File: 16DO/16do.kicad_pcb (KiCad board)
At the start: 2 copper layers, 170 x 80 mm, 70 parts, among them J1 Conn_02x16_Row_Letter_First, J2 CONN_01X16, J3 CONN_01X16, J4 CONN_01X16, J5 CONN_01X16, P1 CONN_01X08, P2 CONN_01X08, P3 CONN_01X08, P4 CONN_01X08, U1 STM32F030CCTx, U13 74HC595, U14 74HC595, U15 74HC595, U16 74HC595, U2 MC33879A, U3 MC33879A, U4 LD3985G33R_TSOT23, U5 AP1117-33, U6 SP3485, U7 SP3485, U8 SP3485, U9 SP3485, Y1 Crystal_GND3

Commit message: finish leds, route most stuff
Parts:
- added C10: 100n, stmbl:C_0603, F.Cu at (90.8, 33.4)
- added C11: 2.2µ, stmbl:C_0603, F.Cu at (86.9, 38.4)
- added C12: 10µ, stmbl:C_0805, F.Cu at (103.4, 65.4)
- added C13: 10µ, stmbl:C_0805, F.Cu at (91.3, 65.0)
- added C14: 100n, stmbl:C_0603, F.Cu at (126.7, 55.6)
- added C15: 2.2µ, stmbl:C_0603, F.Cu at (109.5, 63.4)
- added C16: 10µ, stmbl:C_0805, F.Cu at (101.1, 65.4)
- added C17: 10µ, stmbl:C_0805, F.Cu at (96.8, 83.0)
- added C18: 100n, stmbl:C_0603, F.Cu at (123.2, 64.8)
- added C19: 100n, stmbl:C_0603, F.Cu at (94.5, 33.4)
- added C20: 100n, stmbl:C_0603, F.Cu at (90.5, 38.0)
- added C21: 100n, stmbl:C_0603, F.Cu at (114.4, 54.0)
- added C22: 100n, stmbl:C_0603, F.Cu at (94.5, 35.6)
- added C7: 100n, stmbl:C_0603, F.Cu at (91.3, 57.4)
- added C8: 2.2µ, stmbl:C_0603, F.Cu at (91.3, 56.1)
- added C9: 100n, stmbl:C_0603, F.Cu at (86.0, 60.2)
- added D24: SS34A, stmbl:SMA_Standard, F.Cu at (88.3, 62.8)
- added L1: 4.7µH 1.5A, stmbl:SMD_INDUCTOR_32x25, F.Cu at (91.3, 61.0)
- added MK11: Mounting_Hole, MountingHole:MountingHole_3.2mm_M3, F.Cu at (80.1, 126.0)
- added MK12: Mounting_Hole, MountingHole:MountingHole_3.2mm_M3, F.Cu at (80.1, 54.0)
- added R10: R, stmbl:R_0603, B.Cu at (178.2, 91.0)
- added R11: R, stmbl:R_0603, B.Cu at (178.8, 93.5)
- added R12: R, stmbl:R_0603, B.Cu at (179.5, 91.0)
- added R13: R, stmbl:R_0603, B.Cu at (180.1, 93.5)
- added R14: R, stmbl:R_0603, B.Cu at (180.8, 91.0)
- added R15: R, stmbl:R_0603, B.Cu at (181.4, 93.5)
- added R16: R, stmbl:R_0603, B.Cu at (182.1, 91.0)
- added R17: R, stmbl:R_0603, B.Cu at (178.8, 75.7)
- added R18: R, stmbl:R_0603, B.Cu at (178.1, 62.0)
- added R19: R, stmbl:R_0603, B.Cu at (178.8, 64.6)
- added R20: R, stmbl:R_0603, B.Cu at (179.4, 62.0)
- added R21: R, stmbl:R_0603, B.Cu at (180.1, 64.6)
- added R22: R, stmbl:R_0603, B.Cu at (180.7, 62.0)
- added R23: R, stmbl:R_0603, B.Cu at (181.4, 64.6)
- added R24: R, stmbl:R_0603, B.Cu at (182.0, 62.0)
- added R25: R, stmbl:R_0603, B.Cu at (147.6, 96.8)
- added R26: R, stmbl:R_0603, B.Cu at (147.6, 98.2)
- added R27: R, stmbl:R_0603, B.Cu at (147.6, 103.8)
- added R28: R, stmbl:R_0603, B.Cu at (147.6, 105.2)
- added R29: R, stmbl:R_0603, B.Cu at (147.6, 110.8)
- added R30: R, stmbl:R_0603, B.Cu at (147.6, 112.2)
- added R31: R, stmbl:R_0603, B.Cu at (147.6, 117.8)
- added R32: R, stmbl:R_0603, B.Cu at (147.6, 119.2)
- added R33: R, stmbl:R_0603, B.Cu at (147.6, 62.2)
- added R34: R, stmbl:R_0603, B.Cu at (147.6, 63.6)
- added R35: R, stmbl:R_0603, B.Cu at (147.6, 69.2)
- added R36: R, stmbl:R_0603, B.Cu at (147.6, 70.7)
- added R37: R, stmbl:R_0603, B.Cu at (147.6, 76.2)
- added R38: R, stmbl:R_0603, B.Cu at (147.6, 77.7)
- added R39: R, stmbl:R_0603, B.Cu at (147.6, 83.2)
- added R40: R, stmbl:R_0603, B.Cu at (147.6, 84.7)
- added R41: 10k, stmbl:R_0603, F.Cu at (84.9, 56.9)
- added R42: 51k, stmbl:R_0603, F.Cu at (94.0, 60.5)
- added R43: 1k, stmbl:R_0603, F.Cu at (94.0, 63.2)
- added R9: R, stmbl:R_0603, B.Cu at (178.8, 104.6)
- U15, U16: moved to F.Cu
- U4: value LD3985G33R_TSOT23 -> ACT4088; footprint TO_SOT_Packages_SMD:TSOT-23-5 -> stmbl:SOT-23-6
- moved D12 76.1 mm to (149.6, 117.8), turned to 270 degrees
- moved D11 66.5 mm to (149.6, 110.8), turned to 270 degrees
- moved D10 58.4 mm to (149.6, 103.8), turned to 270 degrees
- moved U15 52.6 mm to (134.8, 93.3), turned to 180 degrees
- moved U16 52.6 mm to (134.9, 86.5), turned to 180 degrees
- moved D9 50.3 mm to (149.6, 96.8), turned to 270 degrees
- moved D16 44.9 mm to (149.6, 83.2), turned to 270 degrees
- moved D15 39.3 mm to (149.6, 76.2), turned to 270 degrees
- moved D14 32.3 mm to (149.6, 69.2), turned to 270 degrees
- moved D13 26.3 mm to (149.6, 62.2), turned to 270 degrees
- moved U5 15.6 mm to (101.1, 59.0), turned to 90 degrees
- moved U14 13.8 mm to (180.4, 70.2), turned to 270 degrees
- moved U4 3.69 mm to (87.7, 57.4)
- moved C3 1.60 mm to (118.5, 74.0)
- moved C5 1.60 mm to (118.5, 108.4)
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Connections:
- C1 pad 2: Net-(C1-Pad2) -> GNDPWR
- C2 pad 2: Net-(C1-Pad2) -> GNDPWR
- D1 pad 3: Net-(D1-Pad3) -> +3V3
- D10 pad 3: Net-(D10-Pad3) -> +3V3
- D11 pad 3: Net-(D10-Pad3) -> +3V3
- D12 pad 3: Net-(D10-Pad3) -> +3V3
- D13 pad 3: Net-(D10-Pad3) -> +3V3
- D14 pad 3: Net-(D10-Pad3) -> +3V3
- D15 pad 3: Net-(D10-Pad3) -> +3V3
- D16 pad 3: Net-(D10-Pad3) -> +3V3
- D18 pad 1: GNDD -> GNDPWR
- D19 pad 1: GNDD -> GNDPWR
- D2 pad 3: Net-(D1-Pad3) -> +3V3
- D20 pad 1: GNDD -> GNDPWR
- D21 pad 1: GNDD -> GNDPWR
- D22 pad 1: GNDD -> GNDPWR
- D23 pad 1: GNDD -> GNDPWR
- D3 pad 3: Net-(D1-Pad3) -> +3V3
- D4 pad 3: Net-(D1-Pad3) -> +3V3
- D5 pad 3: Net-(D1-Pad3) -> +3V3
- D6 pad 3: Net-(D1-Pad3) -> +3V3
- D7 pad 3: Net-(D1-Pad3) -> +3V3
- D8 pad 3: Net-(D1-Pad3) -> +3V3
- D9 pad 3: Net-(D10-Pad3) -> +3V3
- U1 pad 1: Net-(U1-Pad1) -> +3V3
- U1 pad 23: Net-(U1-Pad23) -> GNDPWR
- U1 pad 24: Net-(U1-Pad24) -> +3V3
- U1 pad 35: Net-(U1-Pad35) -> GNDPWR
- U1 pad 36: Net-(U1-Pad36) -> +3V3
- U1 pad 47: Net-(U1-Pad47) -> GNDPWR
- U1 pad 48: Net-(U1-Pad48) -> +3V3
- U1 pad 8: Net-(U1-Pad8) -> GNDPWR
- U1 pad 9: Net-(U1-Pad9) -> +3V3
- U13 pad 1: Net-(D1-Pad1) -> Net-(R10-Pad2)
- U13 pad 15: Net-(D1-Pad2) -> Net-(R9-Pad2)
- U13 pad 2: Net-(D2-Pad2) -> Net-(R11-Pad2)
- U13 pad 3: Net-(D2-Pad1) -> Net-(R12-Pad2)
- U13 pad 4: Net-(D3-Pad2) -> Net-(R13-Pad2)
- U13 pad 5: Net-(D3-Pad1) -> Net-(R14-Pad2)
- U13 pad 6: Net-(D4-Pad2) -> Net-(R15-Pad2)
- U13 pad 7: Net-(D4-Pad1) -> Net-(R16-Pad2)
- U14 pad 1: Net-(D5-Pad1) -> Net-(R18-Pad2)
- U14 pad 15: Net-(D5-Pad2) -> Net-(R17-Pad2)
- U14 pad 2: Net-(D6-Pad2) -> Net-(R19-Pad2)
- U14 pad 3: Net-(D6-Pad1) -> Net-(R20-Pad2)
- U14 pad 4: Net-(D7-Pad2) -> Net-(R21-Pad2)
- U14 pad 5: Net-(D7-Pad1) -> Net-(R22-Pad2)
- U14 pad 6: Net-(D8-Pad2) -> Net-(R23-Pad2)
- U14 pad 7: Net-(D8-Pad1) -> Net-(R24-Pad2)
- U15 pad 1: Net-(D9-Pad1) -> Net-(R31-Pad2)
- U15 pad 15: Net-(D9-Pad2) -> Net-(R32-Pad2)
- U15 pad 2: Net-(D10-Pad2) -> Net-(R30-Pad2)
- U15 pad 3: Net-(D10-Pad1) -> Net-(R29-Pad2)
- U15 pad 4: Net-(D11-Pad2) -> Net-(R28-Pad2)
- U15 pad 5: Net-(D11-Pad1) -> Net-(R27-Pad2)
- U15 pad 6: Net-(D12-Pad2) -> Net-(R26-Pad2)
- U15 pad 7: Net-(D12-Pad1) -> Net-(R25-Pad2)
- U16 pad 1: Net-(D13-Pad1) -> Net-(R39-Pad2)
- U16 pad 15: Net-(D13-Pad2) -> Net-(R40-Pad2)
- U16 pad 2: Net-(D14-Pad2) -> Net-(R38-Pad2)
- U16 pad 3: Net-(D14-Pad1) -> Net-(R37-Pad2)
- U16 pad 4: Net-(D15-Pad2) -> Net-(R36-Pad2)
- U16 pad 5: Net-(D15-Pad1) -> Net-(R35-Pad2)
- U16 pad 6: Net-(D16-Pad2) -> Net-(R34-Pad2)
- U16 pad 7: Net-(D16-Pad1) -> Net-(R33-Pad2)
- U4 pad 2: Net-(U4-Pad2) -> +24V
- U4 pad 5: Net-(U4-Pad5) -> GNDPWR
- U5 pad 1: Net-(U5-Pad1) -> GNDPWR
- U5 pad 2: Net-(U5-Pad2) -> +3V3
- U5 pad 3: Net-(U5-Pad3) -> +5V
- U6 pad 3: GNDD -> GNDPWR
- U6 pad 5: Net-(U6-Pad5) -> GNDPWR
- U7 pad 5: Net-(U7-Pad5) -> GNDPWR
- U8 pad 1: Net-(U8-Pad1) -> DSPI_MOSI
- U8 pad 2: GNDD -> GNDPWR
- U8 pad 4: DSPI_MOSI -> Net-(U8-Pad4)
- U8 pad 5: Net-(U8-Pad5) -> GNDPWR
- U9 pad 1: Net-(U9-Pad1) -> DSPI_SCK
- U9 pad 2: GNDD -> GNDPWR
- U9 pad 4: DSPI_SCK -> Net-(U9-Pad4)
- U9 pad 5: Net-(U9-Pad5) -> GNDPWR
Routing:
- net PWM3: track 0.00 -> 72.1 mm, vias 0 -> 4
- net PWM2: track 0.00 -> 57.1 mm, vias 0 -> 4
- net Net-(D1-Pad2): track 0.00 -> 42.5 mm
- net USART1_RX: track 2.63 -> 45.1 mm
- net Net-(D4-Pad2): track 0.00 -> 42.4 mm
- net Net-(R32-Pad2): track 0.00 -> 40.5 mm, vias 0 -> 1
- net Net-(D1-Pad1): track 0.00 -> 40.2 mm
- net USART1_TX: track 2.63 -> 42.4 mm
- net Net-(D5-Pad2): track 0.00 -> 39.6 mm
- net Net-(D8-Pad2): track 0.00 -> 39.6 mm
- net Net-(D2-Pad2): track 0.00 -> 38.2 mm
- net Net-(R33-Pad2): track 0.00 -> 37.6 mm, vias 0 -> 1
- net USART1_EN: track 5.28 -> 42.7 mm, vias 0 -> 2
- net Net-(R34-Pad2): track 0.00 -> 37.1 mm, vias 0 -> 1
- net Net-(R35-Pad2): track 0.00 -> 36.7 mm, vias 0 -> 1
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- added copper zone on B.Cu, net +24V
- added copper zone on B.Cu, net +3V3
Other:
- board text added: "+ 10 -"
- board text added: "+ 11 -"
- board text added: "+ 12 -"
- board text added: "+ 13 -"
- board text added: "+ 14 -"
- board text added: "+ 15 -"
- board text added: "+ 3 -"
- board text added: "+ 4 -"
- board text added: "+ 5 -"
- board text added: "+ 6 -"
- board text added: "+ 7 -"
- board text added: "+ 8 -"
- board text added: "+ 9 -"
- board text added: "STMBL 16DO main V0.1 dualcolor LED"
- board text added: "STMBL 16xx V0.1 Frontplate"
- board text removed: "STMBL 16DO V0.1 Frontplate"

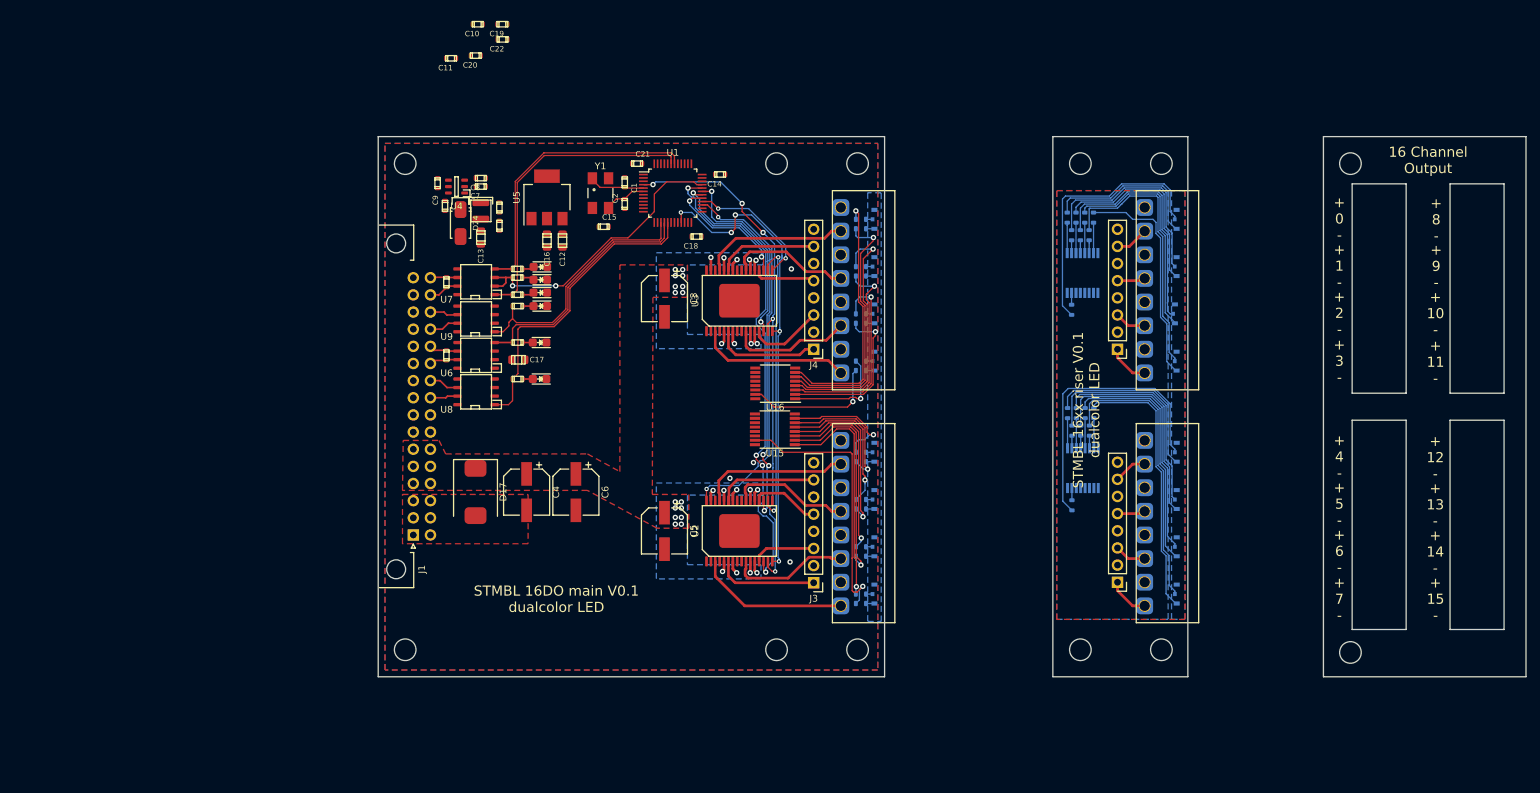
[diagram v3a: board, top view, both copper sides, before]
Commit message: change over to plc bus
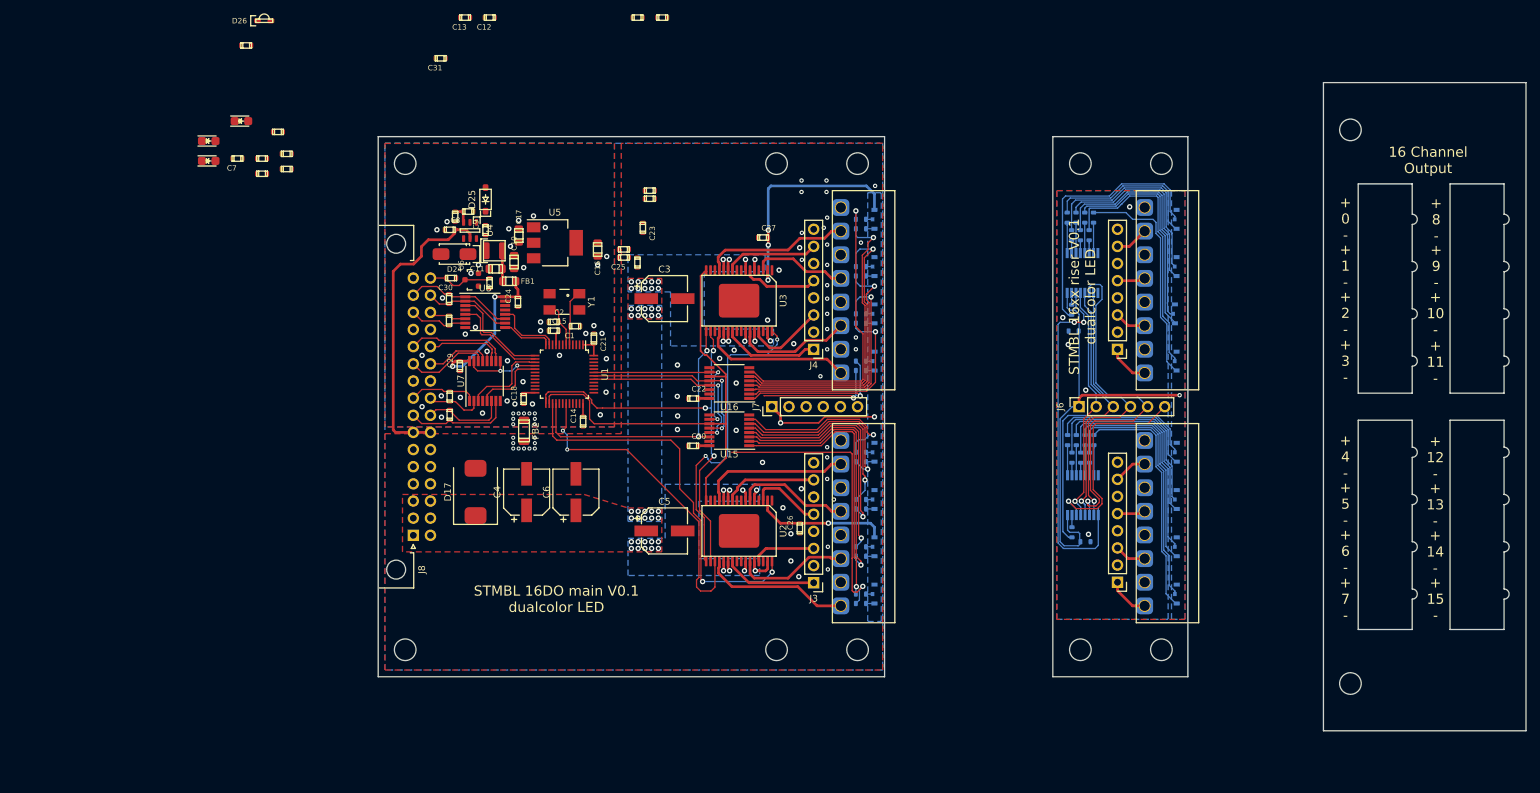
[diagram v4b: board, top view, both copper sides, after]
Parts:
- removed D18, D19, D20: LED, stmbl:LED-0805
- removed J1: Conn_02x16_Row_Letter_First, Connector_DIN:DIN41612_B2_2x16_Horizontal
- removed R1, R5, R6: R, stmbl:R_0603
- removed U9: SP3485, stmbl:SOIC-8-N
- added C23: 100n, stmbl:C_0603, F.Cu at (115.3, 63.5)
- added C24: 100n, stmbl:C_0603, F.Cu at (96.8, 74.5)
- added C25: 100n, stmbl:C_0603, F.Cu at (112.5, 67.9)
- added C26: 100n, stmbl:C_0603, F.Cu at (138.5, 108.0)
- added C27: 100n, stmbl:C_0603, F.Cu at (133.1, 65.0)
- added C28: 100n, stmbl:C_0603, B.Cu at (179.1, 78.8)
- added C29: 100n, stmbl:C_0603, F.Cu at (88.2, 84.0)
- added C30: 1n, stmbl:C_0603, F.Cu at (86.9, 71.0)
- added C31: 1n, stmbl:C_0603, F.Cu at (85.3, 38.4)
- added D25: 1N4148, stmbl:SOD-123, F.Cu at (92.0, 59.3)
- added D26: Led_Small, stmbl:LED-0805-SIDE, F.Cu at (59.2, 32.8)
- added FB1: Ferrite_Bead_Small, stmbl:C_0805, F.Cu at (95.5, 71.4)
- added FB2: Ferrite_Bead_Small, stmbl:C_1206, F.Cu at (97.7, 93.6)
- added J6: CONN_01X06, Connector_PinSocket_2.54mm:PinSocket_1x06_P2.54mm_Vertical, F.Cu at (179.9, 90.0)
- added J7: CONN_01X06, Connector_PinHeader_2.54mm:PinHeader_1x06_P2.54mm_Vertical, F.Cu at (134.4, 90.0)
- added J8: Conn_02x16_Row_Letter_First, Connector_DIN:DIN41612_B2_2x16_Horizontal, F.Cu at (81.3, 109.0)
- added R44: R, stmbl:R_0603, F.Cu at (116.3, 58.0)
- added R45: R, stmbl:R_0603, F.Cu at (116.3, 59.2)
- added R46: 470, stmbl:R_0603, F.Cu at (56.5, 36.5)
- added R48: R, stmbl:R_0603, F.Cu at (114.5, 68.7)
- added R49: R, stmbl:R_0603, F.Cu at (112.5, 66.7)
- added R50: 1k, stmbl:R_0603, F.Cu at (92.6, 71.7)
- added R51: 120, stmbl:R_0603, F.Cu at (86.7, 91.2)
- added R52: 1k, stmbl:R_0603, F.Cu at (86.7, 88.5)
- added R53: 1k, stmbl:R_0603, F.Cu at (86.6, 77.2)
- added R54: 1k, stmbl:R_0603, F.Cu at (114.5, 32.4)
- added R55: 1k, stmbl:R_0603, F.Cu at (118.1, 32.4)
- C1, C2: value C -> 18p
- C10: value 100n -> 10u; footprint stmbl:C_0603 -> stmbl:C_0805
- C11: value 2.2µ -> 10u; footprint stmbl:C_0603 -> stmbl:C_0805
- C12, C13: value 10µ -> 100n; footprint stmbl:C_0805 -> stmbl:C_0603
- C19: moved to B.Cu
- C8: value 2.2µ -> 100n
- D24: value SS34A -> ss110
- L1: value 4.7µH 1.5A -> 22µ 650mA
- R2: value R -> 1k
- R41: value 10k -> R
- R43: value 1k -> 10k
- U4: value ACT4088 -> MCP16331
- U6: value SP3485 -> NFET; footprint stmbl:SOIC-8-N -> stmbl:SOT-23
- U7, U8: value SP3485 -> ADM4168E; footprint stmbl:SOIC-8-N -> Package_SO:TSSOP-16_4.4x5mm_P0.65mm
- moved C19 115.5 mm to (180.8, 110.0)
- moved C20 66.2 mm to (122.7, 95.8), turned to 180 degrees
- moved C22 60.2 mm to (122.7, 88.8), turned to 180 degrees
- moved D23 53.2 mm to (51.0, 50.6), turned to 0 degrees
- moved D21 52.8 mm to (51.0, 53.6), turned to 0 degrees
- moved R4 50.0 mm to (58.9, 53.2)
- moved D22 49.3 mm to (55.8, 47.7), turned to 0 degrees
- moved R3 47.3 mm to (61.2, 49.3)
- moved C14 41.9 mm to (106.4, 92.2), turned to 270 degrees
- moved R7 40.4 mm to (58.9, 55.5)
- moved R8 38.8 mm to (62.5, 52.5)
- moved C7 36.3 mm to (55.2, 53.2)
- moved C10 35.6 mm to (96.2, 68.6), turned to 90 degrees
- moved C18 35.1 mm to (97.6, 88.8), turned to 270 degrees
- moved C12 34.7 mm to (92.6, 32.4), turned to 0 degrees
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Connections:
- net Net-(U1-Pad34) renamed SWDIO
- net Net-(U1-Pad37) renamed SWCLK
- net SPI_MISO renamed SPI2_MISO
- C1 pad 2: GNDPWR -> GND
- C10 pad 2: GNDPWR -> GND
- C11 pad 2: GNDPWR -> GND
- C12 pad 1: +5V -> +5VL
- C12 pad 2: GNDPWR -> GND
- C13 pad 1: +5V -> +5VL
- C13 pad 2: GNDPWR -> GND
- C14 pad 2: GNDPWR -> GND
- C15 pad 2: GNDPWR -> GND
- C16 pad 2: GNDPWR -> GND
- C17 pad 2: GNDPWR -> GND
- C18 pad 2: GNDPWR -> GND
- C2 pad 2: GNDPWR -> GND
- C21 pad 2: GNDPWR -> GND
- C3 pad 1: +24V -> +VDC
- C4 pad 1: +24V -> +VDC
- C5 pad 1: +24V -> +VDC
- C6 pad 1: +24V -> +VDC
- C7 pad 1: +24V -> GNDPWR
- C7 pad 2: GNDPWR -> AIN3
- C8 pad 2: GNDPWR -> GND
- C9 pad 1: Net-(C9-Pad1) -> /Power Supply/BOOST
- C9 pad 2: Net-(C9-Pad2) -> /Power Supply/SW
- D17 pad 1: +24V -> +VDC
- D24 pad 1: Net-(C9-Pad2) -> /Power Supply/SW
- D24 pad 2: GNDPWR -> GND
- L1 pad 1: Net-(C9-Pad2) -> /Power Supply/SW
- R2 pad 1: USART1_A -> UA1+
- R2 pad 2: USART1_B -> UA1-
- R3 pad 1: DSPI_MISO -> +VDC
- R3 pad 2: Net-(D18-Pad2) -> AIN3
- R4 pad 1: DSPI_MOSI -> AIN3
- R4 pad 2: Net-(D19-Pad2) -> GNDPWR
- R41 pad 1: Net-(R41-Pad1) -> USART1_EN
- R41 pad 2: GNDPWR -> Net-(D23-Pad2)
- R42 pad 1: Net-(R42-Pad1) -> +5V
- R42 pad 2: Net-(R41-Pad1) -> /Power Supply/FB
- R43 pad 1: +5V -> /Power Supply/FB
- R43 pad 2: Net-(R42-Pad1) -> GND
- R7 pad 1: USART1_TX -> USART1_RX
- R7 pad 2: Net-(D22-Pad2) -> Net-(D21-Pad2)
- R8 pad 1: USART1_EN -> USART1_TX
- R8 pad 2: Net-(D23-Pad2) -> Net-(D22-Pad2)
- U1 pad 10: AIN0 -> AIN1
- U1 pad 11: AIN1 -> USART_EN
- U1 pad 12: AIN2 -> USART_TX
- U1 pad 13: AIN3 -> USART_RX
- U1 pad 14: Net-(U1-Pad14) -> DSPI_CS
- U1 pad 18: Net-(U1-Pad18) -> AIN2
- U1 pad 19: Net-(U1-Pad19) -> AIN3
- U1 pad 21: SPI_SCK -> Net-(U1-Pad21)
- U1 pad 22: Net-(U1-Pad22) -> DSPI_TXEN
- U1 pad 23: GNDPWR -> GND
- U1 pad 25: Net-(U1-Pad25) -> SPI2_CS
- U1 pad 26: Net-(U1-Pad26) -> SPI2_SCK
- U1 pad 28: SPI_MOSI -> SPI2_MOSI
- U1 pad 33: USART1_EN -> Net-(U1-Pad33)
- U1 pad 35: GNDPWR -> GND
- U1 pad 39: Net-(U1-Pad39) -> EN_OUT
- U1 pad 4: EN_OUT -> Net-(U1-Pad4)
- U1 pad 41: Net-(U1-Pad41) -> OE
- U1 pad 42: USART1_TX -> RCLK
- U1 pad 43: USART1_RX -> SRCLR
- U1 pad 45: Net-(U1-Pad45) -> ESTOP_IN
- U1 pad 46: Net-(U1-Pad46) -> ESTOP_OUT
- U1 pad 47: GNDPWR -> GND
- U1 pad 8: GNDPWR -> GND
- U13 pad 10: Net-(U13-Pad10) -> Net-(J6-Pad4)
- U13 pad 11: Net-(U13-Pad11) -> Net-(J6-Pad5)
- U13 pad 12: Net-(U13-Pad12) -> Net-(J6-Pad3)
- U13 pad 13: Net-(U13-Pad13) -> Net-(J6-Pad2)
- U13 pad 16: Net-(U13-Pad16) -> +3V3
- U14 pad 10: Net-(U14-Pad10) -> Net-(J6-Pad4)
- U14 pad 11: Net-(U14-Pad11) -> Net-(J6-Pad5)
- U14 pad 12: Net-(U14-Pad12) -> Net-(J6-Pad3)
- U14 pad 13: Net-(U14-Pad13) -> Net-(J6-Pad2)
- U14 pad 14: Net-(U14-Pad14) -> Net-(U13-Pad9)
- U14 pad 16: Net-(U14-Pad16) -> +3V3
- U15 pad 10: Net-(U15-Pad10) -> SRCLR
- U15 pad 11: Net-(U15-Pad11) -> SPI2_SCK
- U15 pad 12: Net-(U15-Pad12) -> RCLK
- U15 pad 13: Net-(U15-Pad13) -> OE
- U15 pad 14: Net-(U15-Pad14) -> SPI2_MOSI
- U15 pad 16: Net-(U15-Pad16) -> +3V3
- U16 pad 10: Net-(U16-Pad10) -> SRCLR
- U16 pad 11: Net-(U16-Pad11) -> SPI2_SCK
- U16 pad 12: Net-(U16-Pad12) -> RCLK
- U16 pad 13: Net-(U16-Pad13) -> OE
- U16 pad 14: Net-(U16-Pad14) -> Net-(U15-Pad9)
- U16 pad 16: Net-(U16-Pad16) -> +3V3
- U2 pad 10: OUT1 -> OUT15
- U2 pad 11: +24V -> +VDC
- U2 pad 12: +24V -> +VDC
- U2 pad 13: OUT13 -> OUT3
- U2 pad 16: SPI_SCK -> SPI2_SCK
- U2 pad 18: SPI_CS_OUT -> SPI2_CS
- U2 pad 2: Net-(U2-Pad2) -> +3V3
- U2 pad 20: OUT14 -> OUT0
- U2 pad 21: +24V -> +VDC
- U2 pad 22: +24V -> +VDC
- U2 pad 23: OUT2 -> OUT12
- U2 pad 26: +24V -> +VDC
- U2 pad 27: OUT15 -> OUT1
- U2 pad 28: +24V -> +VDC
- U2 pad 29: OUT3 -> OUT13
- U2 pad 3: OUT0 -> OUT14
- U2 pad 31: +24V -> +VDC
- U2 pad 5: +24V -> +VDC
- U2 pad 6: OUT12 -> OUT2
- U2 pad 7: +24V -> +VDC
- U3 pad 10: OUT5 -> OUT11
- U3 pad 11: +24V -> +VDC
- U3 pad 12: +24V -> +VDC
- U3 pad 13: OUT9 -> OUT7
- U3 pad 16: SPI_SCK -> SPI2_SCK
- U3 pad 17: SPI_MOSI -> SPI2_MOSI
- U3 pad 18: SPI_CS_OUT -> SPI2_CS
- U3 pad 2: Net-(U3-Pad2) -> +3V3
- U3 pad 20: OUT10 -> OUT4
- U3 pad 21: +24V -> +VDC
- U3 pad 22: +24V -> +VDC
- U3 pad 23: OUT6 -> OUT8
- U3 pad 26: +24V -> +VDC
- U3 pad 27: OUT11 -> OUT5
- U3 pad 28: +24V -> +VDC
- U3 pad 29: OUT7 -> OUT9
- U3 pad 3: OUT4 -> OUT6
- U3 pad 31: +24V -> +VDC
- U3 pad 5: +24V -> +VDC
- U3 pad 6: OUT8 -> OUT10
- U3 pad 7: +24V -> +VDC
- U4 pad 1: Net-(C9-Pad2) -> /Power Supply/BOOST
- U4 pad 2: +24V -> GND
- U4 pad 3: Net-(U4-Pad3) -> /Power Supply/FB
- U4 pad 4: Net-(R41-Pad1) -> Net-(U4-Pad4)
- U4 pad 5: GNDPWR -> +24V
- U4 pad 6: Net-(C9-Pad1) -> /Power Supply/SW
- U5 pad 1: GNDPWR -> GND
- U6 pad 1: Net-(U6-Pad1) -> ESTOP_OUT
- U6 pad 2: +3V3 -> GND
- U6 pad 3: GNDPWR -> EST
- U7 pad 1: USART1_RX -> LSC-
- U7 pad 2: USART1_EN -> LSC+
- U7 pad 3: USART1_EN -> DSPI_SCK
- U7 pad 4: USART1_TX -> +5VL
- U7 pad 5: GNDPWR -> DSPI_MOSI
- U7 pad 6: USART1_A -> LSI+
- U7 pad 7: USART1_B -> LSI-
- U7 pad 8: Net-(U7-Pad8) -> GND
- U8 pad 1: DSPI_MOSI -> UA1-
- U8 pad 2: GNDPWR -> UA1+
- U8 pad 3: +3V3 -> USART_RX
- U8 pad 4: Net-(U8-Pad4) -> GND
- U8 pad 5: GNDPWR -> DSPI_CS
- U8 pad 6: DSPI_MOSI_A -> LCS+
- U8 pad 7: DSPI_MOSI_B -> LCS-
- U8 pad 8: Net-(U8-Pad8) -> GND
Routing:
- net +3V3: track 0.00 -> 148.8 mm, vias 0 -> 7
- net EN_OUT: track 77.6 -> 0.00 mm, vias 5 -> 0
- net PWM3: track 72.1 -> 0.00 mm, vias 4 -> 0
- net SPI_SCK: track 71.2 -> 0.00 mm, vias 5 -> 0
- net SPI2_SCK: track 0.00 -> 70.6 mm
- net SPI2_CS: track 0.00 -> 63.4 mm, vias 0 -> 3
- net Net-(J6-Pad5): track 0.00 -> 53.2 mm, vias 0 -> 1
- net Net-(U13-Pad9): track 0.00 -> 53.1 mm, vias 0 -> 2
- net Net-(U2-Pad17): track 0.00 -> 46.0 mm, vias 0 -> 2
- net USART1_RX: track 45.1 -> 0.00 mm
- net SPI2_MOSI: track 0.00 -> 43.5 mm, vias 0 -> 2
- net USART1_EN: track 42.7 -> 0.00 mm, vias 2 -> 0
- net SPI_CS_OUT: track 42.6 -> 0.00 mm, vias 2 -> 0
- net USART1_TX: track 42.4 -> 0.00 mm
- net Net-(J6-Pad4): track 0.00 -> 41.6 mm, vias 0 -> 1
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- added copper zone on B.Cu, net +VDC
- added copper zone on F.Cu, net +VDC
- added copper zone on B.Cu, net GND
- added copper zone on F.Cu, net GND
- removed copper zone on B.Cu, net +24V
- removed copper zone on F.Cu, net +24V
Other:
- board size 170 x 80 mm -> 170 x 96 mm
- net class Power added: clearance 0.15, trace_width 0.4, via_dia 0.8, via_drill 0.4
- net class Small added: clearance 0.15, trace_width 0.15, via_dia 0.6, via_drill 0.3
- rule via_min_size: 0.4 -> 0.6

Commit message: routing
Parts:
- moved R55 69.7 mm to (70.1, 82.9)
- moved C26 1.03 mm to (137.5, 108.0)
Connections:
- U1 pad 39: EN_OUT -> Net-(U1-Pad39)
- U1 pad 40: Net-(U1-Pad40) -> ESTOP_OUT
- U1 pad 46: ESTOP_OUT -> EN_OUT
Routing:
- net +3V3: track 148.8 -> 260.2 mm, vias 7 -> 14
- net EN_OUT: track 0.00 -> 60.7 mm, vias 0 -> 2
- net PWM1: track 0.00 -> 54.3 mm, vias 0 -> 2
- net PWM0: track 0.00 -> 41.9 mm, vias 0 -> 2
- net PWM3: track 0.00 -> 34.8 mm, vias 0 -> 4
- net DSPI_TXEN: track 1.45 -> 12.3 mm, vias 1 -> 2
- net +5VL: track 22.7 -> 29.0 mm, vias 2 -> 3
- net PWM2: track 48.1 -> 51.0 mm
- net SPI2_SCK: track 70.6 -> 72.3 mm
- net +24V: track 45.2 -> 44.0 mm
- net SPI2_CS: track 63.4 -> 64.1 mm
- net Net-(U2-Pad17): track 46.0 -> 45.3 mm
- net DSPI_SCK: track 12.9 -> 13.5 mm
- net SPI2_MOSI: track 43.5 -> 44.0 mm
- net GNDPWR: vias 58 -> 133
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- added copper zone on F.Cu, net /Power Supply/BOOST
- added copper zone on F.Cu, net /Power Supply/SW

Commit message: finish routing and change comms schematic to backplane spec
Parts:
- moved C7 68.3 mm to (113.4, 89.2), turned to 180 degrees
- moved R4 64.6 mm to (113.4, 88.0)
- moved R3 64.2 mm to (113.4, 86.8), turned to 180 degrees
- moved R46 57.1 mm to (108.1, 61.0), turned to 270 degrees
- moved D26 53.6 mm to (105.3, 60.2), turned to 180 degrees
- moved C13 53.2 mm to (87.1, 85.5), turned to 270 degrees
- moved D23 52.4 mm to (101.0, 66.2), turned to 270 degrees
- moved R54 48.0 mm to (100.2, 78.2), turned to 90 degrees
- moved D21 47.9 mm to (97.2, 66.2), turned to 270 degrees
- moved D22 47.1 mm to (99.1, 66.2), turned to 270 degrees
- moved R7 44.7 mm to (96.6, 79.6), turned to 90 degrees
- moved R8 44.4 mm to (97.8, 79.6), turned to 90 degrees
- moved R41 43.3 mm to (99.0, 78.2), turned to 90 degrees
- moved C12 42.4 mm to (98.0, 74.5), turned to 270 degrees
- moved C31 34.4 mm to (93.8, 71.7), turned to 90 degrees
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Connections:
- D21 pad 1: GNDPWR -> GND
- D22 pad 1: GNDPWR -> GND
- D23 pad 1: GNDPWR -> GND
- J8 pad a8: LSI- -> LSC-
- J8 pad a9: LSC- -> LSI-
- J8 pad b8: LSI+ -> LSC+
- J8 pad b9: LSC+ -> LSI+
- R41 pad 1: USART1_EN -> USART_EN
- R51 pad 1: LSI- -> LSC-
- R51 pad 2: LSI+ -> LSC+
- R52 pad 1: LSC- -> LSI-
- R52 pad 2: LSC+ -> LSI+
- R54 pad 1: USART1_EN -> USART_EN
- R7 pad 1: USART1_RX -> USART_RX
- R8 pad 1: USART1_TX -> USART_TX
- U7 pad 1: LSC- -> LSI-
- U7 pad 2: LSC+ -> LSI+
- U7 pad 3: DSPI_SCK -> DSPI_MOSI
- U7 pad 5: DSPI_MOSI -> DSPI_SCK
- U7 pad 6: LSI+ -> LSC+
- U7 pad 7: LSI- -> LSC-
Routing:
- net AIN2: track 0.00 -> 44.3 mm, vias 0 -> 2
- net AIN1: track 0.00 -> 36.9 mm, vias 0 -> 2
- net +5V: track 4.52 -> 38.7 mm
- net Net-(J7-Pad6): track 0.00 -> 26.9 mm, vias 0 -> 1
- net Net-(R40-Pad2): track 17.6 -> 44.3 mm, vias 1 -> 3
- net ESTOP_OUT: track 0.00 -> 26.4 mm, vias 0 -> 2
- net ESTOP_IN: track 0.00 -> 23.5 mm, vias 0 -> 2
- net SRCLR: track 27.0 -> 48.0 mm
- net SPI2_SCK: track 72.3 -> 90.8 mm, vias 0 -> 1
- net AIN3: track 0.00 -> 16.3 mm, vias 0 -> 2
- net RCLK: track 28.4 -> 43.1 mm
- net Net-(D21-Pad2): track 0.00 -> 13.2 mm
- net Net-(D22-Pad2): track 0.00 -> 12.3 mm
- net OE: track 27.4 -> 39.7 mm
- net Net-(D23-Pad2): track 0.00 -> 11.1 mm
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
